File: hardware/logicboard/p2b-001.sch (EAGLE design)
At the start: 71 parts, among them IC1 74LS06N, IC2 4066N, J1 MKR, J3 Vcc, J4*** RLY2, J6 LED, J7 DIN5, J8 DIN5, J9 DIN5, K1 G5V1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

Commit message: Front-side RLY jumper.
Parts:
- J4***: device SparkFun-Connectors:CONN_03JST-PTH -> SparkFun-Connectors:CONN_03JST-PTH-NS
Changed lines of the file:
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@@
 <part name="VCCBRIDGE**" library="rcl" library_urn="urn:adsk.eagle:library:334" deviceset="R-EU_" device="M2012" package3d_urn="urn:adsk.eagle:package:23561/2" value="Inf"/>
 <part name="SUPPLY25" library="supply2" library_urn="urn:adsk.eagle:library:372" deviceset="VCC" device=""/>
-<part name="J4***" library="SparkFun-Connectors" library_urn="urn:adsk.eagle:library:513" deviceset="CONN_03" device="JST-PTH" package3d_urn="urn:adsk.eagle:package:38069/1" value="RLY2"/>
+<part name="J4***" library="SparkFun-Connectors" library_urn="urn:adsk.eagle:library:513" deviceset="CONN_03" device="JST-PTH-NS" package3d_urn="urn:adsk.eagle:package:38084/1" value="RLY2"/>
 <part name="RZ4***" library="rcl" library_urn="urn:adsk.eagle:library:334" deviceset="R-EU_" device="M2012" package3d_urn="urn:adsk.eagle:package:23561/2" value="Inf"/>
 <part name="RZ3***" library="rcl" library_urn="urn:adsk.eagle:library:334" deviceset="R-EU_" device="M2012" package3d_urn="urn:adsk.eagle:package:23561/2" value="Inf"/>

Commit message: Silk.
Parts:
- renumbered JP7 to DISP2, LCD1 to DISP1
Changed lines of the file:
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@@
 <part name="P+1" library="supply1" library_urn="urn:adsk.eagle:library:371" deviceset="VCC/2" device=""/>
 <part name="P+4" library="supply1" library_urn="urn:adsk.eagle:library:371" deviceset="VCC/2" device=""/>
-<part name="JP7" library="pinhead" library_urn="urn:adsk.eagle:library:325" deviceset="PINHD-1X4" device="" package3d_urn="urn:adsk.eagle:package:22407/2" value="MNTR"/>
-<part name="LCD1" library="AQM0802A-RN-GBW" deviceset="AQM0802A-RN-GBW" device=""/>
+<part name="DISP2" library="pinhead" library_urn="urn:adsk.eagle:library:325" deviceset="PINHD-1X4" device="" package3d_urn="urn:adsk.eagle:package:22407/2" value="MNTR"/>
+<part name="DISP1" library="AQM0802A-RN-GBW" deviceset="AQM0802A-RN-GBW" device=""/>
 <part name="R101" library="rcl" library_urn="urn:adsk.eagle:library:334" deviceset="R-EU_" device="M2012" package3d_urn="urn:adsk.eagle:package:23561/2" value="10k"/>
 <part name="R102" library="rcl" library_urn="urn:adsk.eagle:library:334" deviceset="R-EU_" device="M2012" package3d_urn="urn:adsk.eagle:package:23561/2" value="10k"/>
@@
 <attribute name="VALUE" x="203.2" y="121.92" size="1.778" layer="96" rot="R90"/>
 </instance>
-<instance part="JP7" gate="A" x="30.48" y="165.1" smashed="yes" rot="MR0">
+<instance part="DISP2" gate="A" x="30.48" y="165.1" smashed="yes" rot="MR0">
 <attribute name="NAME" x="36.83" y="173.355" size="1.778" layer="95" rot="MR0"/>
 <attribute name="VALUE" x="36.83" y="157.48" size="1.778" layer="96" rot="MR0"/>
 </instance>
-<instance part="LCD1" gate="G$1" x="360.68" y="83.82" smashed="yes">
+<instance part="DISP1" gate="G$1" x="360.68" y="83.82" smashed="yes">
 <attribute name="NAME" x="363.22" y="93.98" size="1.778" layer="95"/>
 <attribute name="VALUE" x="363.22" y="71.12" size="1.778" layer="96"/>
@@
 </segment>
 <segment>
-<pinref part="JP7" gate="A" pin="1"/>
+<pinref part="DISP2" gate="A" pin="1"/>
 <wire x1="33.02" y1="170.18" x2="40.64" y2="170.18" width="0.1524" layer="91"/>
 <label x="40.64" y="170.18" size="0.8128" layer="95" xref="yes"/>
@@
 <segment>
 <pinref part="SUPPLY20" gate="GND" pin="GND"/>
-<pinref part="LCD1" gate="G$1" pin="6"/>
+<pinref part="DISP1" gate="G$1" pin="6"/>
 <wire x1="353.06" y1="81.28" x2="353.06" y2="55.88" width="0.1524" layer="91"/>
 <wire x1="358.14" y1="81.28" x2="353.06" y2="81.28" width="0.1524" layer="91"/>
@@
 </segment>
 <segment>
-<pinref part="JP7" gate="A" pin="2"/>
+<pinref part="DISP2" gate="A" pin="2"/>
 <wire x1="33.02" y1="167.64" x2="40.64" y2="167.64" width="0.1524" layer="91"/>
 <label x="40.64" y="167.64" size="0.8128" layer="95" xref="yes"/>
@@
 </segment>
 <segment>
-<pinref part="JP7" gate="A" pin="4"/>
+<pinref part="DISP2" gate="A" pin="4"/>
 <wire x1="33.02" y1="162.56" x2="40.64" y2="162.56" width="0.1524" layer="91"/>
 <label x="40.64" y="162.56" size="0.8128" layer="95" xref="yes"/>
@@
 <net name="CAP1N" class="0">
 <segment>
-<pinref part="LCD1" gate="G$1" pin="3"/>
+<pinref part="DISP1" gate="G$1" pin="3"/>
 <wire x1="332.74" y1="88.9" x2="358.14" y2="88.9" width="0.1524" layer="91"/>
 <pinref part="C12" gate="G$1" pin="2"/>
@@
 <net name="CAP1P" class="0">
 <segment>
-<pinref part="LCD1" gate="G$1" pin="4"/>
+<pinref part="DISP1" gate="G$1" pin="4"/>
 <wire x1="358.14" y1="86.36" x2="322.58" y2="86.36" width="0.1524" layer="91"/>
 <wire x1="322.58" y1="86.36" x2="322.58" y2="88.9" width="0.1524" layer="91"/>
@@
 <wire x1="332.74" y1="93.98" x2="335.28" y2="93.98" width="0.1524" layer="91"/>
 <wire x1="335.28" y1="93.98" x2="335.28" y2="91.44" width="0.1524" layer="91"/>
-<pinref part="LCD1" gate="G$1" pin="2"/>
+<pinref part="DISP1" gate="G$1" pin="2"/>
 <wire x1="335.28" y1="91.44" x2="358.14" y2="91.44" width="0.1524" layer="91"/>
 <pinref part="C13" gate="G$1" pin="2"/>
@@
 </segment>
 <segment>
-<pinref part="JP7" gate="A" pin="3"/>
+<pinref part="DISP2" gate="A" pin="3"/>
 <wire x1="33.02" y1="165.1" x2="40.64" y2="165.1" width="0.1524" layer="91"/>
 <label x="40.64" y="165.1" size="0.8128" layer="95" xref="yes"/>
@@
 <net name="SDA3V" class="0">
 <segment>
-<pinref part="LCD1" gate="G$1" pin="7"/>
+<pinref part="DISP1" gate="G$1" pin="7"/>
 <wire x1="358.14" y1="78.74" x2="294.64" y2="78.74" width="0.1524" layer="91"/>
 <pinref part="R104" gate="G$1" pin="1"/>
@@
 <wire x1="325.12" y1="93.98" x2="320.04" y2="93.98" width="0.1524" layer="91"/>
 <wire x1="320.04" y1="93.98" x2="320.04" y2="83.82" width="0.1524" layer="91"/>
-<pinref part="LCD1" gate="G$1" pin="5"/>
+<pinref part="DISP1" gate="G$1" pin="5"/>
 <wire x1="358.14" y1="83.82" x2="335.28" y2="83.82" width="0.1524" layer="91"/>
 <junction x="335.28" y="83.82"/>
 <wire x1="335.28" y1="83.82" x2="335.28" y2="73.66" width="0.1524" layer="91"/>
 <wire x1="335.28" y1="73.66" x2="335.28" y2="66.04" width="0.1524" layer="91"/>
-<pinref part="LCD1" gate="G$1" pin="9"/>
+<pinref part="DISP1" gate="G$1" pin="9"/>
 <wire x1="358.14" y1="73.66" x2="335.28" y2="73.66" width="0.1524" layer="91"/>
 <junction x="335.28" y="73.66"/>
@@
 <wire x1="281.94" y1="71.12" x2="284.48" y2="71.12" width="0.1524" layer="91"/>
 <wire x1="284.48" y1="71.12" x2="284.48" y2="76.2" width="0.1524" layer="91"/>
-<pinref part="LCD1" gate="G$1" pin="8"/>
+<pinref part="DISP1" gate="G$1" pin="8"/>
 <wire x1="358.14" y1="76.2" x2="284.48" y2="76.2" width="0.1524" layer="91"/>
 <label x="345.44" y="76.2" size="1.778" layer="95"/>

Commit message: Silk.
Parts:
- renumbered J4*** to J4**, RZ1** to RZ1***, RZ2** to RZ2***, RZ3*** to RZ3**, RZ4*** to RZ4**, VCCBRIDGE** to VCCBRIDGE***
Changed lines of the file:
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@@
 <part name="Q1" library="SparkFun-DiscreteSemi" library_urn="urn:adsk.eagle:library:514" deviceset="MOSFET-NCH" device="-BSS138" package3d_urn="urn:adsk.eagle:package:38446/1" value="220mA/50V/3.5Ω"/>
 <part name="Q2" library="SparkFun-DiscreteSemi" library_urn="urn:adsk.eagle:library:514" deviceset="MOSFET-NCH" device="-BSS138" package3d_urn="urn:adsk.eagle:package:38446/1" value="220mA/50V/3.5Ω"/>
-<part name="RZ1**" library="rcl" library_urn="urn:adsk.eagle:library:334" deviceset="R-EU_" device="M2012" package3d_urn="urn:adsk.eagle:package:23561/2" value="Inf"/>
-<part name="RZ2**" library="rcl" library_urn="urn:adsk.eagle:library:334" deviceset="R-EU_" device="M2012" package3d_urn="urn:adsk.eagle:package:23561/2" value="Inf"/>
+<part name="RZ1***" library="rcl" library_urn="urn:adsk.eagle:library:334" deviceset="R-EU_" device="M2012" package3d_urn="urn:adsk.eagle:package:23561/2" value="Inf"/>
+<part name="RZ2***" library="rcl" library_urn="urn:adsk.eagle:library:334" deviceset="R-EU_" device="M2012" package3d_urn="urn:adsk.eagle:package:23561/2" value="Inf"/>
 <part name="SUPPLY22" library="supply2" library_urn="urn:adsk.eagle:library:372" deviceset="VCC" device=""/>
 <part name="SUPPLY24" library="supply2" library_urn="urn:adsk.eagle:library:372" deviceset="VCC" device=""/>
 <part name="VDDBRIDGE" library="rcl" library_urn="urn:adsk.eagle:library:334" deviceset="R-EU_" device="M2012" package3d_urn="urn:adsk.eagle:package:23561/2" value="0"/>
-<part name="VCCBRIDGE**" library="rcl" library_urn="urn:adsk.eagle:library:334" deviceset="R-EU_" device="M2012" package3d_urn="urn:adsk.eagle:package:23561/2" value="Inf"/>
+<part name="VCCBRIDGE***" library="rcl" library_urn="urn:adsk.eagle:library:334" deviceset="R-EU_" device="M2012" package3d_urn="urn:adsk.eagle:package:23561/2" value="Inf"/>
 <part name="SUPPLY25" library="supply2" library_urn="urn:adsk.eagle:library:372" deviceset="VCC" device=""/>
-<part name="J4***" library="SparkFun-Connectors" library_urn="urn:adsk.eagle:library:513" deviceset="CONN_03" device="JST-PTH-NS" package3d_urn="urn:adsk.eagle:package:38084/1" value="RLY2"/>
-<part name="RZ4***" library="rcl" library_urn="urn:adsk.eagle:library:334" deviceset="R-EU_" device="M2012" package3d_urn="urn:adsk.eagle:package:23561/2" value="Inf"/>
-<part name="RZ3***" library="rcl" library_urn="urn:adsk.eagle:library:334" deviceset="R-EU_" device="M2012" package3d_urn="urn:adsk.eagle:package:23561/2" value="Inf"/>
+<part name="J4**" library="SparkFun-Connectors" library_urn="urn:adsk.eagle:library:513" deviceset="CONN_03" device="JST-PTH-NS" package3d_urn="urn:adsk.eagle:package:38084/1" value="RLY2"/>
+<part name="RZ4**" library="rcl" library_urn="urn:adsk.eagle:library:334" deviceset="R-EU_" device="M2012" package3d_urn="urn:adsk.eagle:package:23561/2" value="Inf"/>
+<part name="RZ3**" library="rcl" library_urn="urn:adsk.eagle:library:334" deviceset="R-EU_" device="M2012" package3d_urn="urn:adsk.eagle:package:23561/2" value="Inf"/>
 <part name="J2" library="SparkFun-Connectors" library_urn="urn:adsk.eagle:library:513" deviceset="CONN_04" device="JST-PTH" package3d_urn="urn:adsk.eagle:package:38101/1"/>
 <part name="J5" library="SparkFun-Connectors" library_urn="urn:adsk.eagle:library:513" deviceset="CONN_06" device="1.27MM" package3d_urn="urn:adsk.eagle:package:38131/1"/>
@@
 <attribute name="VALUE" x="279.4" y="109.22" size="1.778" layer="96" font="vector" rot="MR270"/>
 </instance>
-<instance part="RZ1**" gate="G$1" x="276.86" y="71.12" smashed="yes">
+<instance part="RZ1***" gate="G$1" x="276.86" y="71.12" smashed="yes">
 <attribute name="NAME" x="273.05" y="72.6186" size="1.778" layer="95"/>
 <attribute name="VALUE" x="273.05" y="67.818" size="1.778" layer="96"/>
 </instance>
-<instance part="RZ2**" gate="G$1" x="276.86" y="106.68" smashed="yes">
+<instance part="RZ2***" gate="G$1" x="276.86" y="106.68" smashed="yes">
 <attribute name="NAME" x="273.05" y="108.1786" size="1.778" layer="95"/>
 <attribute name="VALUE" x="273.05" y="103.378" size="1.778" layer="96"/>
@@
 <attribute name="VALUE" x="323.342" y="100.33" size="1.778" layer="96" rot="R90"/>
 </instance>
-<instance part="VCCBRIDGE**" gate="G$1" x="312.42" y="104.14" smashed="yes" rot="R90">
+<instance part="VCCBRIDGE***" gate="G$1" x="312.42" y="104.14" smashed="yes" rot="R90">
 <attribute name="NAME" x="310.9214" y="100.33" size="1.778" layer="95" rot="R90"/>
 <attribute name="VALUE" x="315.722" y="100.33" size="1.778" layer="96" rot="R90"/>
@@
 <attribute name="VALUE" x="312.42" y="119.38" size="1.778" layer="96" align="bottom-center"/>
 </instance>
-<instance part="J4***" gate="J$1" x="111.76" y="50.8" smashed="yes">
+<instance part="J4**" gate="J$1" x="111.76" y="50.8" smashed="yes">
 <attribute name="VALUE" x="111.76" y="43.18" size="1.778" layer="96" align="bottom-center"/>
 <attribute name="NAME" x="111.76" y="55.88" size="1.778" layer="95" align="bottom-center"/>
 </instance>
-<instance part="RZ4***" gate="G$1" x="124.46" y="220.98" smashed="yes" rot="R90">
+<instance part="RZ4**" gate="G$1" x="124.46" y="220.98" smashed="yes" rot="R90">
 <attribute name="NAME" x="122.9614" y="217.17" size="1.778" layer="95" rot="R90"/>
 <attribute name="VALUE" x="127.762" y="217.17" size="1.778" layer="96" rot="R90"/>
 </instance>
-<instance part="RZ3***" gate="G$1" x="137.16" y="220.98" smashed="yes" rot="R90">
+<instance part="RZ3**" gate="G$1" x="137.16" y="220.98" smashed="yes" rot="R90">
 <attribute name="NAME" x="135.6614" y="217.17" size="1.778" layer="95" rot="R90"/>
 <attribute name="VALUE" x="140.462" y="217.17" size="1.778" layer="96" rot="R90"/>
@@
 </segment>
 <segment>
-<pinref part="VCCBRIDGE**" gate="G$1" pin="2"/>
+<pinref part="VCCBRIDGE***" gate="G$1" pin="2"/>
 <pinref part="SUPPLY25" gate="G$1" pin="VCC"/>
 <wire x1="312.42" y1="109.22" x2="312.42" y2="111.76" width="0.1524" layer="91"/>
@@
 <wire x1="269.24" y1="111.76" x2="269.24" y2="106.68" width="0.1524" layer="91"/>
 <junction x="269.24" y="111.76"/>
-<pinref part="RZ2**" gate="G$1" pin="1"/>
+<pinref part="RZ2***" gate="G$1" pin="1"/>
 <wire x1="269.24" y1="106.68" x2="271.78" y2="106.68" width="0.1524" layer="91"/>
 <wire x1="269.24" y1="111.76" x2="266.7" y2="111.76" width="0.1524" layer="91"/>
@@
 <junction x="104.14" y="210.82"/>
 <label x="104.14" y="210.82" size="1.778" layer="95"/>
-<pinref part="RZ4***" gate="G$1" pin="1"/>
+<pinref part="RZ4**" gate="G$1" pin="1"/>
 <wire x1="124.46" y1="215.9" x2="124.46" y2="213.36" width="0.1524" layer="91"/>
 <wire x1="124.46" y1="213.36" x2="114.3" y2="213.36" width="0.1524" layer="91"/>
@@
 <wire x1="106.68" y1="215.9" x2="106.68" y2="208.28" width="0.1524" layer="91"/>
 <junction x="106.68" y="208.28"/>
-<pinref part="RZ3***" gate="G$1" pin="1"/>
+<pinref part="RZ3**" gate="G$1" pin="1"/>
 <wire x1="137.16" y1="213.36" x2="137.16" y2="215.9" width="0.1524" layer="91"/>
 <wire x1="137.16" y1="213.36" x2="132.08" y2="213.36" width="0.1524" layer="91"/>
@@
 <wire x1="119.38" y1="48.26" x2="121.92" y2="48.26" width="0.1524" layer="91"/>
 <label x="121.92" y="48.26" size="0.8128" layer="95" xref="yes"/>
-<pinref part="J4***" gate="J$1" pin="1"/>
+<pinref part="J4**" gate="J$1" pin="1"/>
 </segment>
 </net>
@@
 <label x="266.7" y="76.2" size="0.8128" layer="95" rot="R180" xref="yes"/>
 <wire x1="269.24" y1="76.2" x2="269.24" y2="71.12" width="0.1524" layer="91"/>
-<pinref part="RZ1**" gate="G$1" pin="1"/>
+<pinref part="RZ1***" gate="G$1" pin="1"/>
 <wire x1="269.24" y1="71.12" x2="271.78" y2="71.12" width="0.1524" layer="91"/>
 </segment>
@@
 <pinref part="R104" gate="G$1" pin="1"/>
 <wire x1="284.48" y1="114.3" x2="284.48" y2="111.76" width="0.1524" layer="91"/>
-<pinref part="RZ2**" gate="G$1" pin="2"/>
+<pinref part="RZ2***" gate="G$1" pin="2"/>
 <wire x1="284.48" y1="111.76" x2="284.48" y2="106.68" width="0.1524" layer="91"/>
 <wire x1="284.48" y1="106.68" x2="281.94" y2="106.68" width="0.1524" layer="91"/>
@@
 <wire x1="312.42" y1="93.98" x2="320.04" y2="93.98" width="0.1524" layer="91"/>
 <label x="345.44" y="83.82" size="1.778" layer="95"/>
-<pinref part="VCCBRIDGE**" gate="G$1" pin="1"/>
+<pinref part="VCCBRIDGE***" gate="G$1" pin="1"/>
 <wire x1="312.42" y1="99.06" x2="312.42" y2="93.98" width="0.1524" layer="91"/>
 <pinref part="VDDBRIDGE" gate="G$1" pin="1"/>
@@
 <wire x1="284.48" y1="78.74" x2="284.48" y2="76.2" width="0.1524" layer="91"/>
 <junction x="284.48" y="76.2"/>
-<pinref part="RZ1**" gate="G$1" pin="2"/>
+<pinref part="RZ1***" gate="G$1" pin="2"/>
 <wire x1="281.94" y1="71.12" x2="284.48" y2="71.12" width="0.1524" layer="91"/>
 <wire x1="284.48" y1="71.12" x2="284.48" y2="76.2" width="0.1524" layer="91"/>
@@
 <net name="RLYOUT2" class="0">
 <segment>
-<pinref part="RZ4***" gate="G$1" pin="2"/>
+<pinref part="RZ4**" gate="G$1" pin="2"/>
 <wire x1="124.46" y1="226.06" x2="124.46" y2="228.6" width="0.1524" layer="91"/>
 <label x="124.46" y="228.6" size="0.8128" layer="95" rot="R90" xref="yes"/>
@@
 <wire x1="121.92" y1="53.34" x2="119.38" y2="53.34" width="0.1524" layer="91"/>
 <label x="121.92" y="53.34" size="0.8128" layer="95" xref="yes"/>
-<pinref part="J4***" gate="J$1" pin="3"/>
+<pinref part="J4**" gate="J$1" pin="3"/>
 </segment>
 </net>
 <net name="RLYOUT1" class="0">
 <segment>
-<pinref part="RZ3***" gate="G$1" pin="2"/>
+<pinref part="RZ3**" gate="G$1" pin="2"/>
 <wire x1="137.16" y1="226.06" x2="137.16" y2="228.6" width="0.1524" layer="91"/>
 <label x="137.16" y="228.6" size="0.8128" layer="95" rot="R90" xref="yes"/>
@@
 <wire x1="119.38" y1="50.8" x2="121.92" y2="50.8" width="0.1524" layer="91"/>
 <label x="121.92" y="50.8" size="0.8128" layer="95" xref="yes"/>
-<pinref part="J4***" gate="J$1" pin="2"/>
-</segment>
-</net>
+<pinref part="J4**" gate="J$1" pin="2"/>
+</segment>
+</net>

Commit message: Silk.
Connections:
- net N$1 renamed MTRTNRAW
- net N$2 renamed MORTNRAW
- net N$6 renamed MO2RTNRAW
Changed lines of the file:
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@@
 </segment>
 </net>
-<net name="N$2" class="0">
+<net name="MORTNRAW" class="0">
 <segment>
 <pinref part="RN4" gate="D" pin="1"/>
@@
 </segment>
 </net>
-<net name="N$1" class="0">
+<net name="MTRTNRAW" class="0">
 <segment>
 <pinref part="RN4" gate="F" pin="1"/>
@@
 </segment>
 </net>
-<net name="N$6" class="0">
+<net name="MO2RTNRAW" class="0">
 <segment>
 <pinref part="RN4" gate="H" pin="1"/>

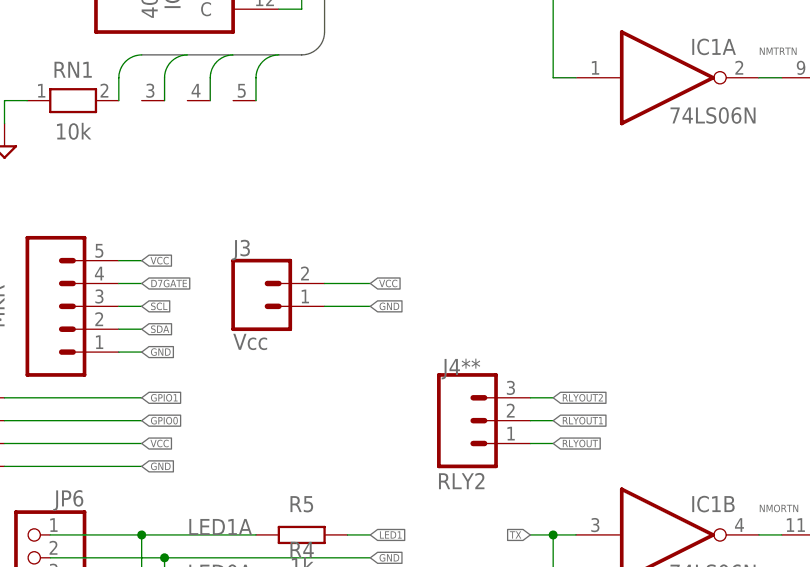
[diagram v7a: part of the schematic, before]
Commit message: J3 is now Voutraw conn.
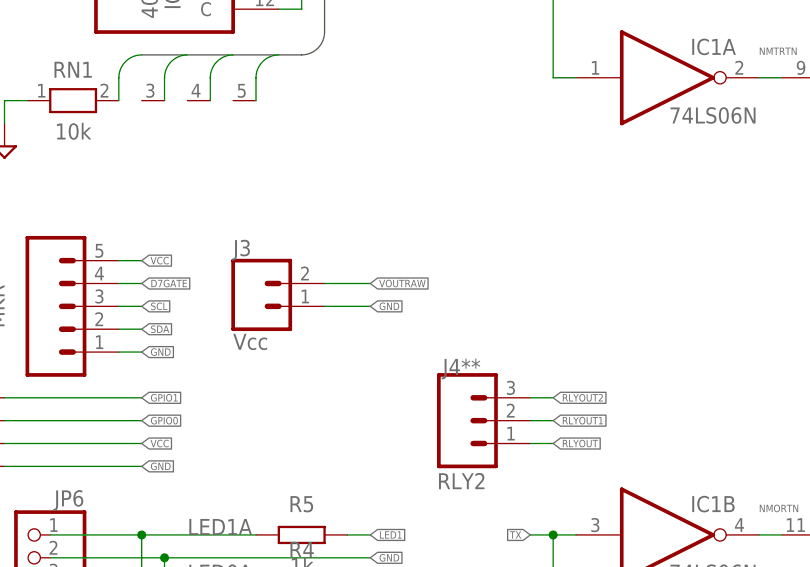
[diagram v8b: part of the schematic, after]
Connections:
- net VCC: no longer J3.2
- net VOUTRAW: now also J3.2
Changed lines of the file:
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@@
-</segment>
-<segment>
-<wire x1="96.52" y1="66.04" x2="101.6" y2="66.04" width="0.1524" layer="91"/>
-<pinref part="J3" gate="G$1" pin="2"/>
-<label x="101.6" y="66.04" size="0.8128" layer="95" xref="yes"/>
 </segment>
 <segment>
@@
 <junction x="132.08" y="213.36"/>
 </segment>
-</net>
+<segment>
+<wire x1="96.52" y1="66.04" x2="101.6" y2="66.04" width="0.1524" layer="91"/>
+<pinref part="J3" gate="G$1" pin="2"/>
+<label x="101.6" y="66.04" size="0.8128" layer="95" xref="yes"/>
+</segment>
+</net>
